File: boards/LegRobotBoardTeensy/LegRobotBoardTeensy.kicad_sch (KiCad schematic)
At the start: 179 parts, among them J1 IDC, J10 IDC, J11 IDC, J12 IDC, J13 IDC, J14 IDC, J15 IDC, J16 IDC, J17 Conn_01x05, J18 Conn_01x05, J19 Conn_01x05, J2 B3B-XH-A, J20 Conn_01x05, J21 Conn_01x05, J22 Conn_01x05, J23 Conn_01x05, J24 Conn_01x05, J3 B3B-XH-A, J4 B3B-XH-A, J5 B3B-XH-A, J6 IDC, J7 IDC, J8 IDC, J9 IDC, Q1 AO3400A, Q10 AO3400A, Q11 AO3400A, Q12 AO3400A, Q13 AO3400A, Q14 AO3400A, Q15 AO3400A, Q16 AO3400A, Q17 AO3400A, Q18 AO3400A, Q19 AO3400A, Q2 AO3400A, Q20 AO3400A, Q21 AO3400A, Q22 AO3400A, Q23 AO3400A, Q24 AO3400A, Q3 AO3400A, Q4 AO3400A, Q5 AO3400A, Q6 AO3400A, Q7 AO3400A, Q8 AO3400A, Q9 AO3400A, U1 Teensy4.0, U11 IS31FL3739-GRLS4-TR, U2 TLC555CDR, U3 SN74HC08DR, U4 SN74HC08DR, U5 PCA9685PW_118, U6 SN74HC08DR, U7 SN74HC08DR, U8 BNO055

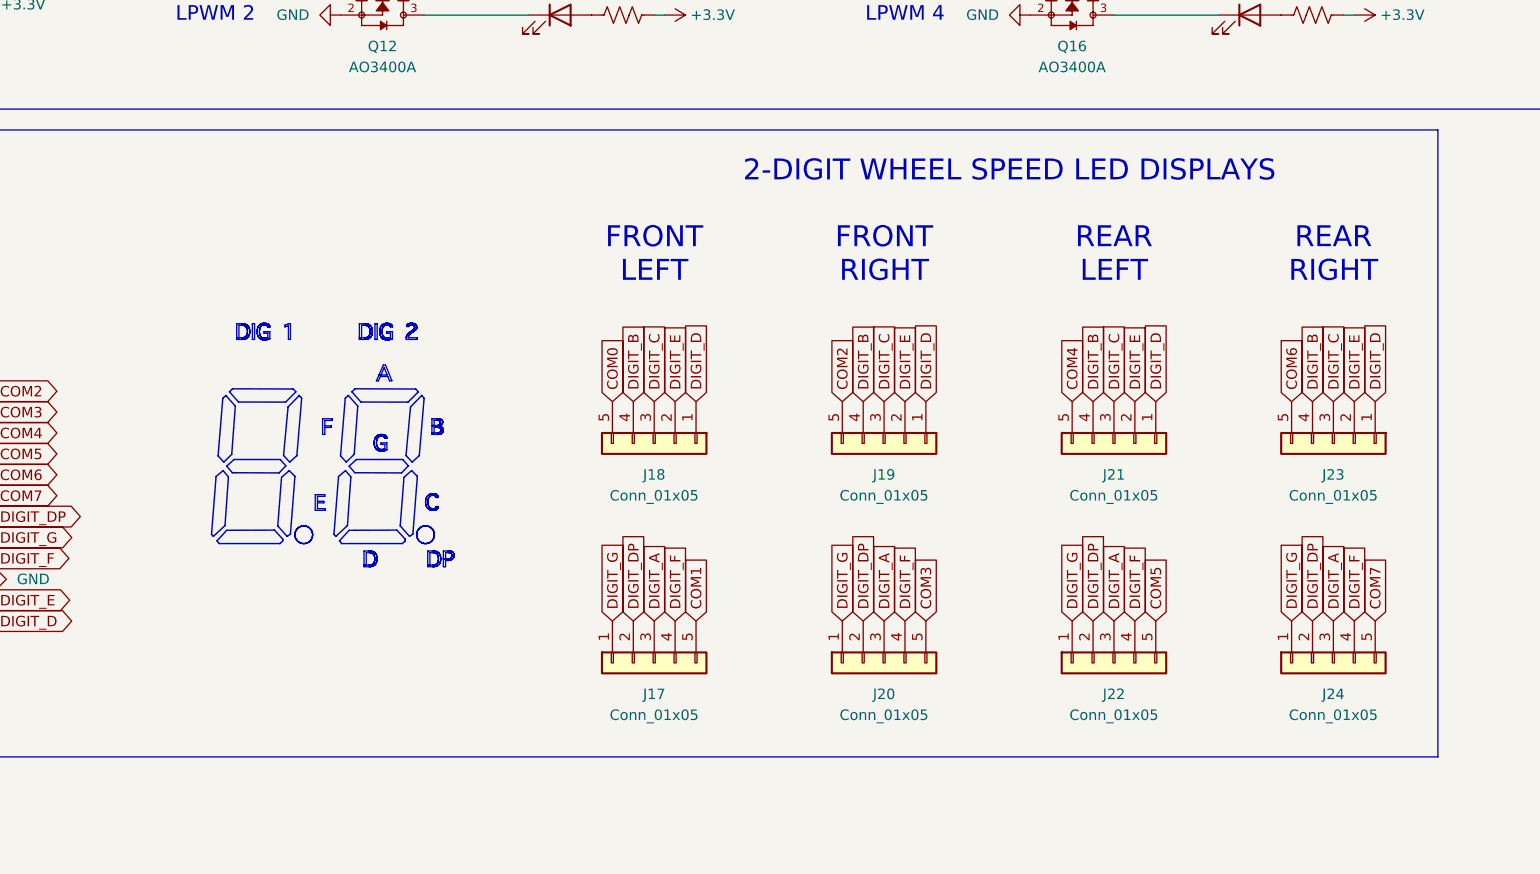
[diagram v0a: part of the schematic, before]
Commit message: Leg board re-do LED displays, main board prepare for re-routing
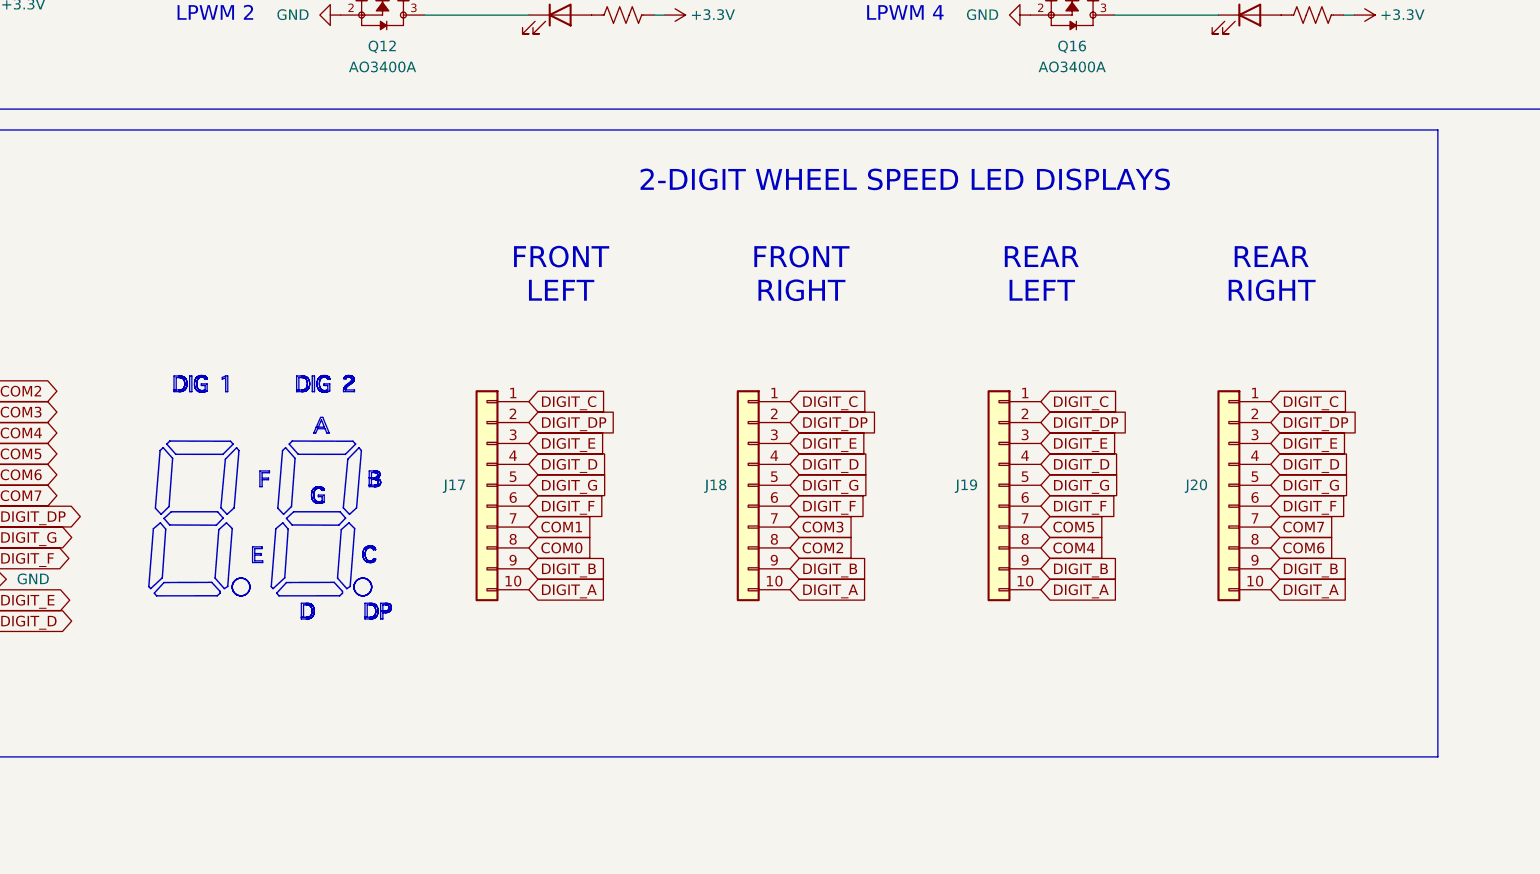
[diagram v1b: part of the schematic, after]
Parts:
- removed J17, J18, J19, J20, J21, J22, J23, J24: Conn_01x05, Connector_PinHeader_2.54mm:PinHeader_1x05_P2.54mm_Vertical, symbol Connector_Generic:Conn_01x05
- added J17, J18, J19, J20: Conn_01x10, DIP:DIP-10_W15.24mm, symbol Connector_Generic:Conn_01x10
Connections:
- net COM0: now also J17.8 (Pin_8)
- net COM1: now also J17.7 (Pin_7)
- net COM2: now also J18.8 (Pin_8)
- net COM3: now also J18.7 (Pin_7)
- net COM4: now also J19.8 (Pin_8)
- net COM5: now also J19.7 (Pin_7)
- net COM6: now also J20.8 (Pin_8)
- net COM7: now also J20.7 (Pin_7)
- net DIGIT_A: now also J17.10 (Pin_10), J18.10 (Pin_10), J19.10 (Pin_10), J20.10 (Pin_10)
- net DIGIT_B: now also J17.9 (Pin_9), J18.9 (Pin_9), J19.9 (Pin_9), J20.9 (Pin_9)
- net DIGIT_C: now also J17.1 (Pin_1), J18.1 (Pin_1), J19.1 (Pin_1), J20.1 (Pin_1)
- net DIGIT_D: now also J17.4 (Pin_4), J18.4 (Pin_4), J19.4 (Pin_4), J20.4 (Pin_4)
- net DIGIT_DP: now also J17.2 (Pin_2), J18.2 (Pin_2), J19.2 (Pin_2), J20.2 (Pin_2)
- net DIGIT_E: now also J17.3 (Pin_3), J18.3 (Pin_3), J19.3 (Pin_3), J20.3 (Pin_3)
- net DIGIT_F: now also J17.6 (Pin_6), J18.6 (Pin_6), J19.6 (Pin_6), J20.6 (Pin_6)
- net DIGIT_G: now also J17.5 (Pin_5), J18.5 (Pin_5), J19.5 (Pin_5), J20.5 (Pin_5)

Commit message: Re-finalize leg board
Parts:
- removed R27: 10K, CRCW060310K0FKEA:CRCW060310K0FKEA, symbol Device:R_US
- removed U1: Teensy4.0, Teensy40:Teensy40, symbol Teensy:Teensy4.0
- removed U5: PCA9685PW_118, PCA9685PW,118:PCA9685PW,118, symbol PCA9685PW,118:PCA9685PW_118
- added U1: Teensy4.1, Teensy4.1:Teensy41, symbol Teensy4.1:Teensy4.1
- D1, D2, D3, D4, D5, D6, D7, D8: footprint NCD0603R1:NCD0603R1 -> XL-1608SURC-06:XL-1608SURC-06; LCSC C84263 -> C965799
- J17, J18, J19, J20: footprint DIP:DIP-10_W15.24mm -> Package_DIP:DIP-10_W10.16mm
- R10, R3, R4, R5, R6, R7, R8, R9: value 1K -> 470R; footprint RCG06031K00FKEA:RCG06031K00FKEA -> RC0603FR-07470RL:RC0603FR-07470RL; LCSC C4264491 -> C114669
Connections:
- net +3.3V: now also U1.15 (3V3), U1.51 (3V3)
- net COM0: now also J17.10 (Pin_10); no longer J17.8 (Pin_8)
- net COM1: now also J17.5 (Pin_5); no longer J17.7 (Pin_7)
- net COM2: now also J18.10 (Pin_10); no longer J18.8 (Pin_8)
- net COM3: now also J18.5 (Pin_5); no longer J18.7 (Pin_7)
- net COM4: now also J19.10 (Pin_10); no longer J19.8 (Pin_8)
- net COM5: now also J19.5 (Pin_5); no longer J19.7 (Pin_7)
- net COM6: now also J20.10 (Pin_10); no longer J20.8 (Pin_8)
- net COM7: now also J20.5 (Pin_5); no longer J20.7 (Pin_7)
- net DIGIT_A: now also J17.3 (Pin_3), J18.3 (Pin_3), J19.3 (Pin_3), J20.3 (Pin_3); no longer J17.10 (Pin_10), J18.10 (Pin_10), J19.10 (Pin_10), J20.10 (Pin_10)
- net DIGIT_C: now also J17.8 (Pin_8), J18.8 (Pin_8), J19.8 (Pin_8), J20.8 (Pin_8); no longer J17.1 (Pin_1), J18.1 (Pin_1), J19.1 (Pin_1), J20.1 (Pin_1)
- net DIGIT_D: now also J17.6 (Pin_6), J18.6 (Pin_6), J19.6 (Pin_6), J20.6 (Pin_6); no longer J17.4 (Pin_4), J18.4 (Pin_4), J19.4 (Pin_4), J20.4 (Pin_4)
- net DIGIT_E: now also J17.7 (Pin_7), J18.7 (Pin_7), J19.7 (Pin_7), J20.7 (Pin_7); no longer J17.3 (Pin_3), J18.3 (Pin_3), J19.3 (Pin_3), J20.3 (Pin_3)
- net DIGIT_F: now also J17.4 (Pin_4), J18.4 (Pin_4), J19.4 (Pin_4), J20.4 (Pin_4); no longer J17.6 (Pin_6), J18.6 (Pin_6), J19.6 (Pin_6), J20.6 (Pin_6)
- net DIGIT_G: now also J17.1 (Pin_1), J18.1 (Pin_1), J19.1 (Pin_1), J20.1 (Pin_1); no longer J17.5 (Pin_5), J18.5 (Pin_5), J19.5 (Pin_5), J20.5 (Pin_5)
- net ENCODER1_A: now also U1.24 (32_OUT1B)
- net ENCODER1_B: now also U1.25 (33_MCLK2)
- net ENCODER1_I: now also U1.44 (22_A8_CTX1)
- net ENCODER2_A: now also U1.26 (34_RX8)
- net ENCODER2_B: now also U1.27 (35_TX8)
- net ENCODER2_I: now also U1.45 (23_A9_CRX1_MCLK1)
- net ENCODER3_A: now also U1.28 (36_CS)
- net ENCODER3_B: now also U1.29 (37_CS)
- net ENCODER3_I: now also U1.16 (24_A10_TX6_SCL2)
- net ENCODER4_A: now also U1.30 (38_CS1_IN1)
- net ENCODER4_B: now also U1.31 (39_MISO1_OUT1A)
- net ENCODER4_I: now also U1.17 (25_A11_RX6_SDA2)
- net GND: now also U1.1 (GND), U1.34 (GND), U1.47 (GND), U1.52 (GND)
- net LPWM1: now also U1.3 (1_TX1_CTX2_MISO1)
- net LPWM2: now also U1.5 (3_LRCLK2)
- net LPWM3: now also U1.7 (5_IN2)
- net LPWM4: now also U1.9 (7_RX2_OUT1A)
- net LPWM5: now also U1.11 (9_OUT1C)
- net LPWM6: now also U1.13 (11_MOSI_CTX1)
- net LPWM7: now also U1.35 (13_SCK_LED)
- net LPWM8: now also U1.37 (15_A1_RX3_SPDIF_IN)
- net PWMEN1: now also U1.18 (26_A12_MOSI1)
- net PWMEN2: now also U1.19 (27_A13_SCK1)
- net PWMEN3: now also U1.20 (28_RX7)
- net PWMEN4: now also U1.21 (29_TX7)
- net PWMEN5: now also U1.22 (30_CRX3)
- net PWMEN6: now also U1.23 (31_CTX3)
- net PWMEN7: now also U1.42 (20_A6_TX5_LRCLK1)
- net PWMEN8: now also U1.43 (21_A7_RX5_BCLK1)
- net RPWM1: now also U1.2 (0_RX1_CRX2_CS1)
- net RPWM2: now also U1.4 (2_OUT2)
- net RPWM3: now also U1.6 (4_BCLK2)
- net RPWM4: now also U1.8 (6_OUT1D)
- net RPWM5: now also U1.10 (8_TX2_IN1)
- net RPWM6: now also U1.12 (10_CS_MQSR)
- net RPWM7: now also U1.14 (12_MISO_MQSL)
- net RPWM8: now also U1.36 (14_A0_TX3_SPDIF_OUT)
- net SCL: now also U1.41 (19_A5_SCL)
- net SDA: now also U1.40 (18_A4_SDA)
- net A0 renamed POT1
- net POT1: now also U1.32 (40_A16)
- net A1 renamed POT2
- net POT2: now also U1.33 (41_A17)
- net A2 renamed POT3
- net POT3: now also U1.38 (16_A2_RX4_SCL1)
- net A3 renamed POT4
- net POT4: now also U1.39 (17_A3_TX4_SDA1)
- no-connect marks 30 -> 23
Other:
- note removed: "PWM DRIVER"
- moved on the sheet: C1, C2, C3, C4, D10, D11, D12, D13, D14, D15, D16, D17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
